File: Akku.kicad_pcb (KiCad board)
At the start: 2 copper layers, 56 parts, among them P1 CONN_01X01, P10 CONN_01X01, P11 CONN_01X01, P2 CONN_01X01, P3 CONN_01X01, P4 CONN_01X01, P5 CONN_01X01, P6 CONN_01X01, P7 CONN_02X10, P8 CONN_02X10, P9 CONN_02X10, SW1 UP_Bonsai_SWITCH_INV, SW2 DOWN_Bonsai_SWITCH_INV, SW3 CLR_Bonsai_SWITCH_INV, U1 74HC14, U2 7400, U3 74HC14, U4 7408, U5 74LS193, U6 74LS541, U7 74LS193, U8 74LS540

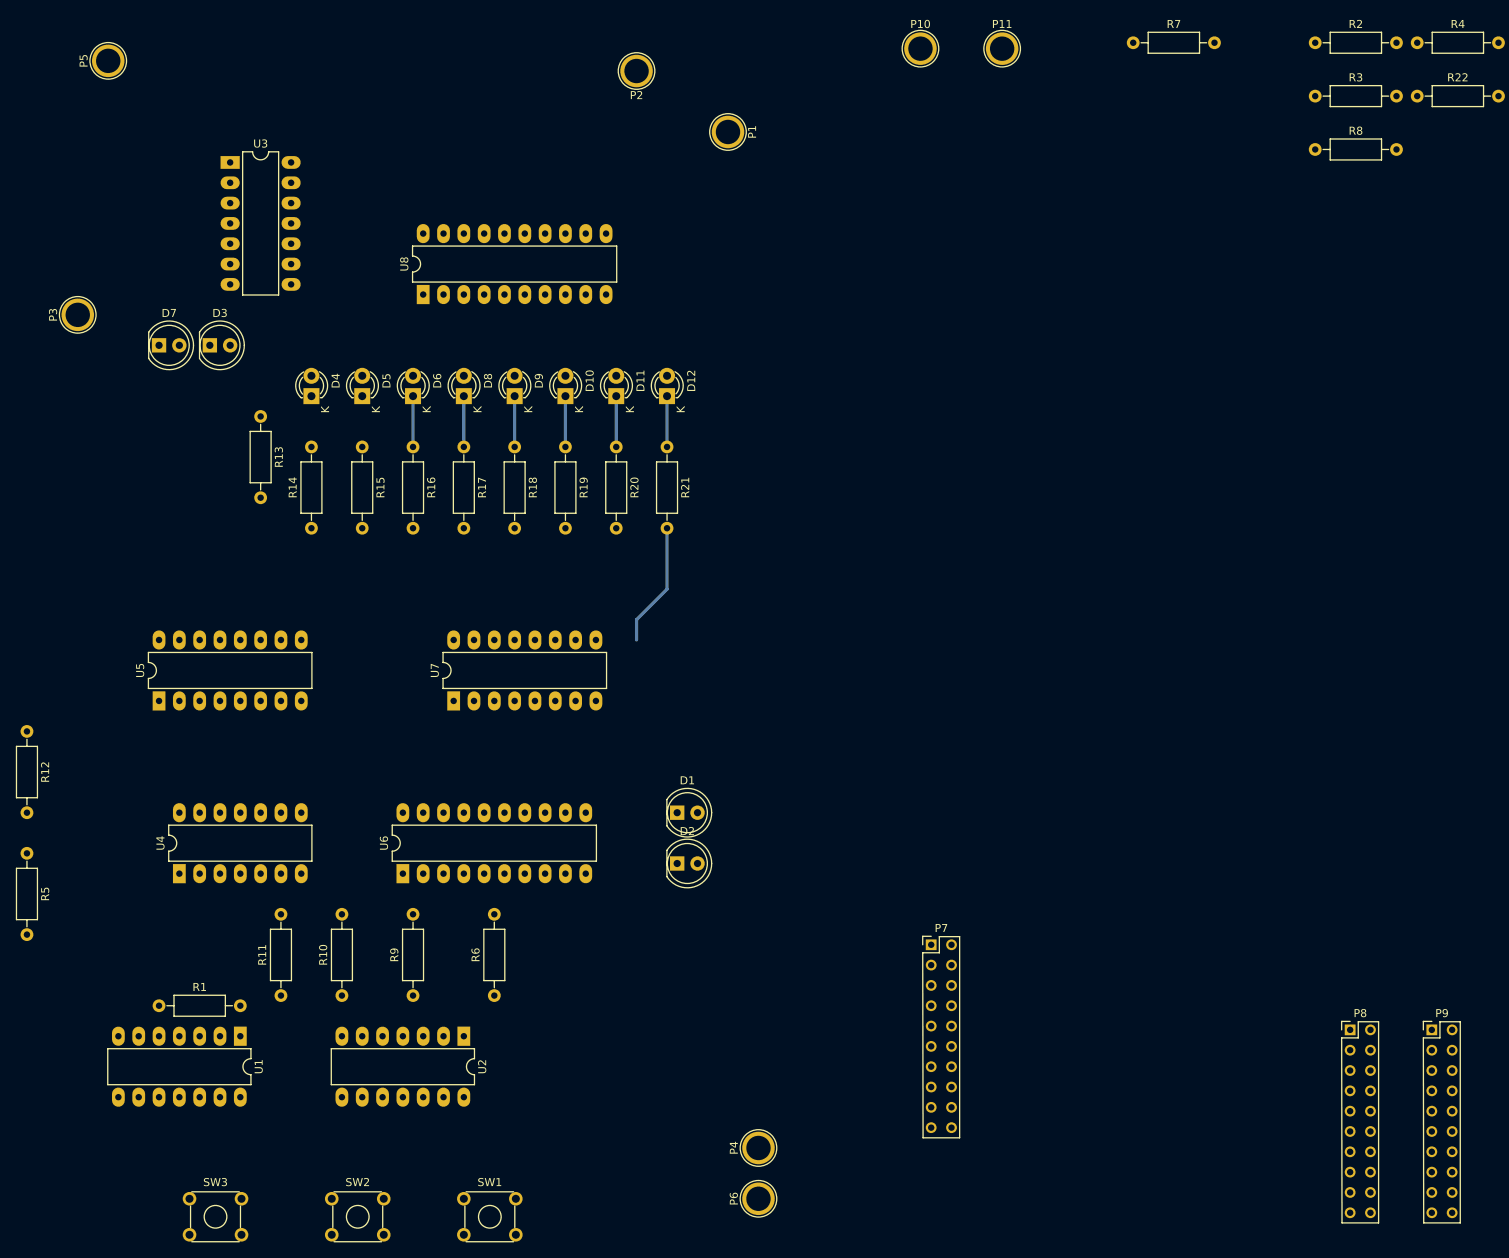
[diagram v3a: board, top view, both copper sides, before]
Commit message: footprint problem behoben falsche todo list gelöscht etc.
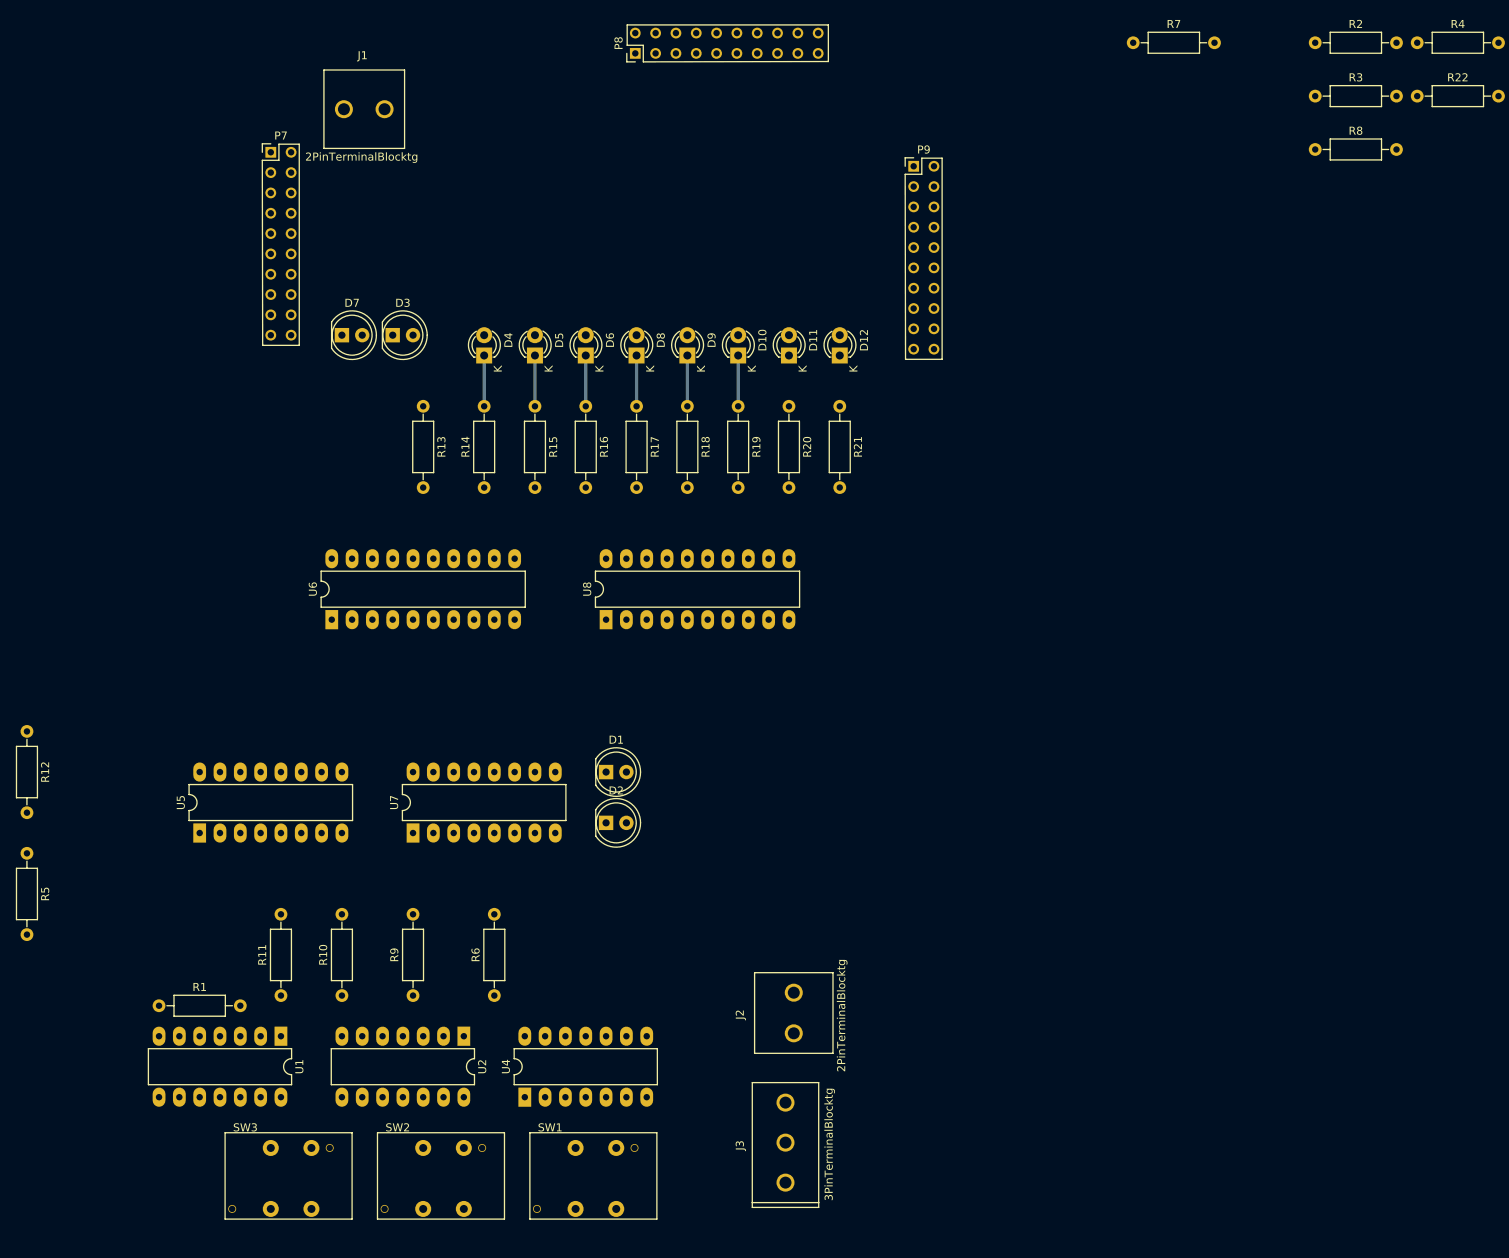
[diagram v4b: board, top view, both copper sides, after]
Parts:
- removed P1, P10, P11, P2, P3, P4, P5, P6: CONN_01X01, Connect:1pin
- removed U3: 74HC14, Housings_DIP:DIP-14_W7.62mm_LongPads
- added J1: 2PinTerminalBlocktg, 2PinTerminalBlocktg, F.Cu at (96.8, 68.3)
- added J2: 2PinTerminalBlocktg, 2PinTerminalBlocktg, F.Cu at (150.5, 181.2)
- added J3: 3PinTerminalBlocktg, 3PinTerminalBlocktg, F.Cu at (149.4, 197.4)
- SW1, SW2, SW3: footprint Buttons_Switches_ThroughHole:SW_TH_Tactile_Omron_B3F-10xx -> tg_foodprint:SW_PUSH_LCD_E3_SAxxxx_tg
- moved P8 151.3 mm to (130.7, 61.3), turned to 90 degrees
- moved P7 128.9 mm to (85.1, 73.7)
- moved P9 125.9 mm to (165.4, 75.4)
- moved U4 51.4 mm to (116.8, 191.8)
- moved U8 46.6 mm to (127.0, 132.1)
- moved U6 33.0 mm to (92.7, 132.1)
- moved D3 22.9 mm to (100.3, 96.5)
- moved D7 22.9 mm to (94.0, 96.5)
- moved R14 22.2 mm to (111.8, 115.6)
- moved D11 22.2 mm to (149.9, 99.1)
- moved D12 22.2 mm to (156.2, 99.1)
- moved D4 22.2 mm to (111.8, 99.1)
- moved D5 22.2 mm to (118.1, 99.1)
- moved D8 22.2 mm to (130.8, 99.1)
- moved D9 22.2 mm to (137.2, 99.1)
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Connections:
- net CLR renamed Net-(J2-Pad2)
- net down renamed Net-(J3-Pad1)
- net enable renamed Net-(J3-Pad3)
- net load renamed Net-(J2-Pad1)
- net up renamed Net-(J3-Pad2)
- U1 pad 10: (no net) -> Net-(R11-Pad1)
- U1 pad 11: (no net) -> Net-(U1-Pad11)
- U1 pad 12: (no net) -> Net-(R10-Pad1)
- U1 pad 13: (no net) -> Net-(U1-Pad13)
- U1 pad 3: Net-(U1-Pad3) -> Net-(U1-Pad2)
- U1 pad 4: Net-(R10-Pad1) -> Net-(U1-Pad4)
- U1 pad 5: Net-(U1-Pad5) -> Net-(U1-Pad4)
- U4 pad 11: Net-(U1-Pad3) -> Net-(U1-Pad13)
- U4 pad 3: Net-(U3-Pad5) -> Net-(U1-Pad11)
- U5 pad 4: Net-(U1-Pad3) -> Net-(U1-Pad13)
- U5 pad 5: Net-(U3-Pad5) -> Net-(U1-Pad11)
- U6 pad 1: Net-(U1-Pad5) -> Net-(U1-Pad4)
- U6 pad 19: Net-(U1-Pad5) -> Net-(U1-Pad4)
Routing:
- net Net-(R21-Pad2): track 15.5 -> 0.00 mm
- net Net-(D6-Pad1): track 6.35 -> 12.7 mm
- net Net-(D5-Pad1): track 0.00 -> 6.35 mm
- net Net-(D12-Pad1): track 6.35 -> 0.00 mm
- net Net-(D11-Pad1): track 6.35 -> 0.00 mm

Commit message: austauschprozess
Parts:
- added REF**: EuroBoard160mmX100mm_holes, EuroBoard_Outline:EuroBoard160mmX100mm_holes, F.Cu at (139.7, 237.5)
- J1: value 2PinTerminalBlocktg -> +/- Stecker
- J2: value 2PinTerminalBlocktg -> load/up
- J3: value 3PinTerminalBlocktg -> down/en/clear
- moved R22 190.9 mm to (120.0, 223.7), turned to 90 degrees
- moved D9 152.2 mm to (288.3, 81.3)
- moved R18 152.2 mm to (288.3, 87.6)
- moved R6 152.2 mm to (264.2, 161.3)
- moved R7 152.2 mm to (344.0, 42.2)
- moved U4 152.2 mm to (268.0, 174.0)
- moved D1 152.2 mm to (278.1, 133.3)
- moved D10 152.2 mm to (294.6, 81.3)
- moved D11 152.2 mm to (301.0, 81.3)
- moved D2 152.2 mm to (278.1, 139.7)
- moved D4 152.2 mm to (262.9, 81.3)
- moved D5 152.2 mm to (269.2, 81.3)
- moved D6 152.2 mm to (275.6, 81.3)
- moved D8 152.2 mm to (281.9, 81.3)
- moved R1 152.2 mm to (222.2, 162.6)
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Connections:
- SW1 pad 0: (no net) -> GND
- SW1 pad 1: Net-(R4-Pad2) -> Net-(R5-Pad2)
- SW1 pad 2: GND -> Net-(R4-Pad2)
- SW2 pad 0: (no net) -> GND
- SW2 pad 1: Net-(R7-Pad2) -> Net-(R6-Pad1)
- SW2 pad 2: GND -> Net-(R7-Pad2)
- SW3 pad 0: (no net) -> Net-(R12-Pad2)
- SW3 pad 1: GND -> VCC
- SW3 pad 2: Net-(R12-Pad2) -> GND
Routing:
- net Net-(D6-Pad1): track 12.7 -> 6.35 mm
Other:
- board outline added: 100 x 160 mm

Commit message: footprint fertig ausgetauscht
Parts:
- moved R2 208.5 mm to (178.8, 132.4)
- moved R3 208.5 mm to (178.8, 139.0)
- moved R4 208.5 mm to (191.6, 132.4)
- moved R7 208.5 mm to (156.1, 132.4)
- moved R8 208.5 mm to (178.8, 145.7)
- moved D1 177.8 mm to (104.1, 170.2)
- moved D11 177.8 mm to (127.0, 118.1)
- moved D2 177.8 mm to (104.1, 176.5)
- moved D5 177.8 mm to (95.2, 118.1)
- moved D8 177.8 mm to (108.0, 118.1)
- moved D9 177.8 mm to (114.3, 118.1)
- moved R1 177.8 mm to (48.3, 199.4)
- moved R10 177.8 mm to (71.1, 198.1)
- moved R11 177.8 mm to (63.5, 198.1)
- moved R13 177.8 mm to (81.3, 124.5)
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
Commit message: diverse Vorbereitungen für akku, switch update
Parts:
- SW1, SW2, SW3: footprint tg_foodprint:SW_PUSH_LCD_E3_SAxxxx_tg -> tg_foodprint:SW_PUSH_LCD_E3_SAxxxx_tg_V2
- moved SW3 31.1 mm to (102.8, 195.0)
- moved D10 8.52 mm to (113.0, 121.9)
- moved D11 8.52 mm to (119.4, 121.9)
- moved D4 8.52 mm to (81.3, 121.9)
- moved D5 8.52 mm to (87.6, 121.9)
- moved D8 8.52 mm to (100.3, 121.9)
- moved D12 8.52 mm to (125.7, 121.9)
- moved D6 8.52 mm to (94.0, 121.9)
- moved D9 8.52 mm to (106.7, 121.9)
- moved D3 8.38 mm to (59.7, 118.9)
- moved D7 8.38 mm to (53.3, 118.9)
- moved R15 7.62 mm to (87.6, 124.7)
- moved R17 7.62 mm to (100.3, 124.7)
- moved R19 7.62 mm to (113.0, 124.7)
- moved R20 7.62 mm to (119.4, 124.7)
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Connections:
- J3 pad 1: Net-(J3-Pad1) -> RPAVCC
- P7 pad 1: Net-(P7-Pad1) -> (no net)
- P7 pad 10: Net-(P7-Pad10) -> (no net)
- P7 pad 2: Net-(P7-Pad2) -> (no net)
- P7 pad 3: Net-(P7-Pad3) -> (no net)
- P7 pad 4: Net-(P7-Pad4) -> (no net)
- P7 pad 5: Net-(P7-Pad5) -> (no net)
- P7 pad 6: Net-(P7-Pad6) -> (no net)
- P7 pad 7: Net-(P7-Pad7) -> (no net)
- P7 pad 8: Net-(P7-Pad8) -> (no net)
- P7 pad 9: Net-(P7-Pad9) -> (no net)
- P8 pad 1: Net-(P8-Pad1) -> (no net)
- P8 pad 10: Net-(P8-Pad10) -> (no net)
- P8 pad 2: Net-(P8-Pad2) -> (no net)
- P8 pad 3: Net-(P8-Pad3) -> (no net)
- P8 pad 4: Net-(P8-Pad4) -> (no net)
- P8 pad 5: Net-(P8-Pad5) -> (no net)
- P8 pad 6: Net-(P8-Pad6) -> (no net)
- P8 pad 7: Net-(P8-Pad7) -> (no net)
- P8 pad 8: Net-(P8-Pad8) -> (no net)
- P8 pad 9: Net-(P8-Pad9) -> (no net)
- P9 pad 10: Net-(P9-Pad10) -> (no net)
- P9 pad 2: Net-(P9-Pad2) -> (no net)
- P9 pad 3: Net-(P9-Pad3) -> (no net)
- P9 pad 4: Net-(P9-Pad4) -> (no net)
- P9 pad 5: Net-(P9-Pad5) -> (no net)
- P9 pad 6: Net-(P9-Pad6) -> (no net)
- P9 pad 7: Net-(P9-Pad7) -> (no net)
- P9 pad 8: Net-(P9-Pad8) -> (no net)
- P9 pad 9: Net-(P9-Pad9) -> (no net)
- R8 pad 2: Net-(J3-Pad1) -> (no net)
- SW2 pad 2: Net-(R7-Pad2) -> RPA2
- U2 pad 12: Net-(R7-Pad2) -> RPA2
- U4 pad 13: Net-(J3-Pad1) -> RPAVCC
- U7 pad 12: Net-(U7-Pad12) -> (no net)
- U7 pad 13: Net-(U7-Pad13) -> (no net)
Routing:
- net Net-(D9-Pad1): track 6.35 -> 0.00 mm
- net Net-(D8-Pad1): track 6.35 -> 0.00 mm
- net Net-(D6-Pad1): track 6.35 -> 0.00 mm
- net Net-(D5-Pad1): track 6.35 -> 0.00 mm
- net Net-(D10-Pad1): track 6.35 -> 0.00 mm

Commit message: akku todos
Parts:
- added RPA1: R_PACK4BUSSED, tg_locallibs:R_Array_SIP5, F.Cu at (123.1, 165.3)
- added RPB1: R_PACK4BUSSED, tg_locallibs:R_Array_SIP5, F.Cu at (123.1, 169.6)
- moved SW3 31.3 mm to (99.3, 226.1)
- moved P9 1.78 mm to (131.8, 90.2)
- moved P8 1.70 mm to (104.1, 84.6)
- moved J2 1.27 mm to (134.1, 208.5)
- moved P7 1.27 mm to (45.2, 90.2)
- moved J3 0.18 mm to (134.1, 221.7)
- moved R22 0.09 mm to (119.9, 223.7)
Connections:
- R7 pad 2: Net-(R7-Pad2) -> (no net)
